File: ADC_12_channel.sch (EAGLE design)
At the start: 165 parts, among them K1 691131710003, K2 691101710002, K3 691101710002, K4 691101710002, K5 691101710002, K6 691101710002, K7 691101710002, K8 691101710002, K9 691101710002, U1 AD7864ASZ-1, U10 TL082D, U11 +12v, U12 V_REG_317SMD, U2 AD7864ASZ-1, U3 TL082D, U4 TL082D, U5 TL082D, U6 TL082D, U7 TL082D, U8 TL082D, U9 TL082D, X1 QTE-040

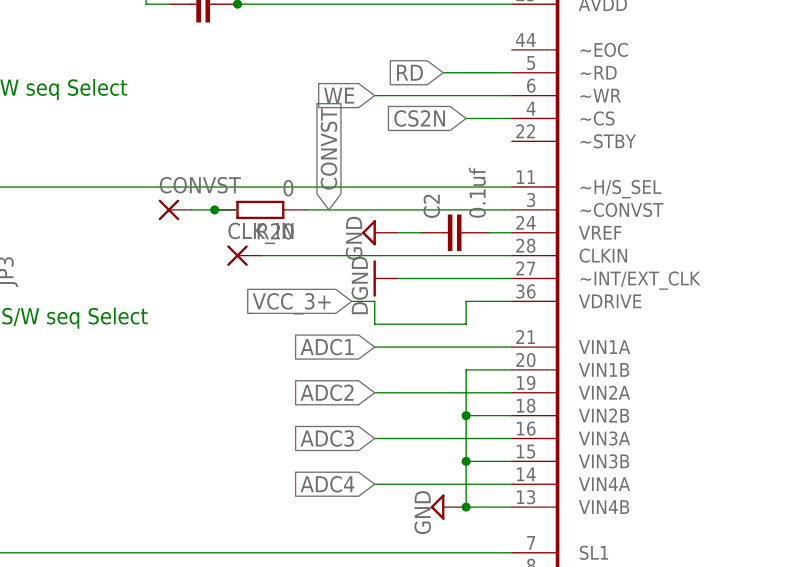
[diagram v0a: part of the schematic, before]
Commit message: Added CLK INT/EXT resistor & relocated inout Opamp
Reducing the size
created possibility to input external clock
relocated the Omapms to reduce the board size.
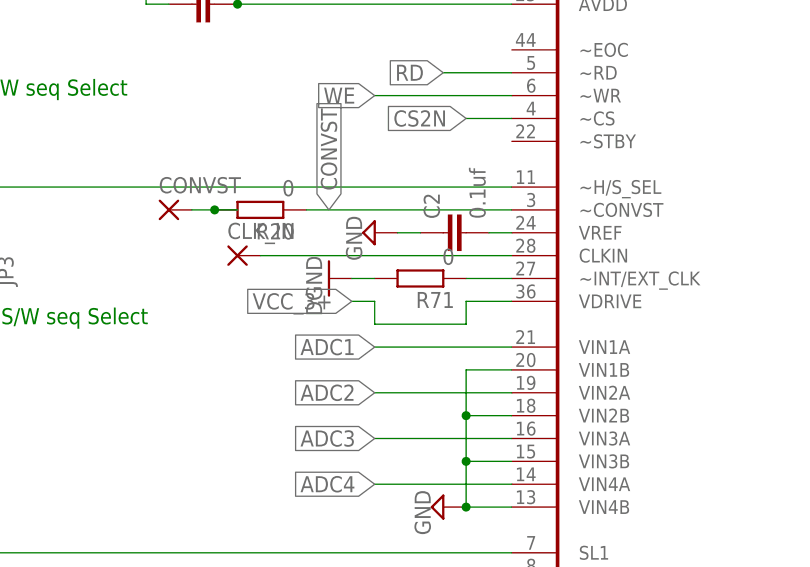
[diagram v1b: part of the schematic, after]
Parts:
- added R71: 0, resistor:R-EU_M1206
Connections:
- new net N$47: R71.1, U1.~INT/EXT_CLK
- net DGND: now also R71.2; no longer U1.~INT/EXT_CLK
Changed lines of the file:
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@@
 <part name="CONVST" library="wirepad" deviceset="3,17/1,3" device=""/>
 <part name="R20" library="resistor" deviceset="R-EU_" device="M1206" value="0"/>
+<part name="R71" library="resistor" deviceset="R-EU_" device="M1206" value="0"/>
 </parts>
 <sheets>
@@
 <instance part="AGND1" gate="GND" x="20.32" y="2.54" rot="R270"/>
 <instance part="AGND2" gate="GND" x="17.78" y="27.94" rot="R270"/>
-<instance part="GND6" gate="1" x="10.16" y="53.34" rot="R270"/>
+<instance part="GND6" gate="1" x="5.08" y="53.34" rot="R270"/>
 <instance part="SUPPLY3" gate="GND" x="10.16" y="58.42" rot="R270"/>
 <instance part="U$1" gate="G$1" x="617.22" y="274.32"/>
@@
 <instance part="CONVST" gate="1" x="-12.7" y="60.96"/>
 <instance part="R20" gate="G$1" x="-2.54" y="60.96" rot="R180"/>
+<instance part="R71" gate="G$1" x="15.24" y="53.34" rot="R180"/>
 </instances>
 <busses>
@@
 </segment>
 <segment>
-<pinref part="U1" gate="A" pin="~INT/EXT_CLK"/>
-<wire x1="25.4" y1="53.34" x2="12.7" y2="53.34" width="0.1524" layer="91"/>
-<pinref part="GND6" gate="1" pin="GND"/>
-</segment>
-<segment>
 <pinref part="C11" gate="G$1" pin="2"/>
 <pinref part="SUPPLY9" gate="GND" pin="GND"/>
@@
 <pinref part="SUPPLY18" gate="GND" pin="GND"/>
 <wire x1="-269.24" y1="-22.86" x2="-269.24" y2="-27.94" width="0.1524" layer="91"/>
+</segment>
+<segment>
+<pinref part="R71" gate="G$1" pin="2"/>
+<pinref part="GND6" gate="1" pin="GND"/>
+<wire x1="10.16" y1="53.34" x2="7.62" y2="53.34" width="0.1524" layer="91"/>
 </segment>
 </net>
@@
 </segment>
 </net>
+<net name="N$47" class="0">
+<segment>
+<pinref part="R71" gate="G$1" pin="1"/>
+<pinref part="U1" gate="A" pin="~INT/EXT_CLK"/>
+<wire x1="20.32" y1="53.34" x2="25.4" y2="53.34" width="0.1524" layer="91"/>
+</segment>
+</net>

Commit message: Removed unnecessary component Adjusted the location of ADC opamps Realigned Processors!! Very criticall
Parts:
- removed JP4: (no value), SparkFun-Retired:JUMPER-2PTH
- removed PAD2, PAD3: WIREPAD1,6/0,8, wirepad:WIREPAD1,6/0,8
- added R72: 0, resistor:R-EU_M1206
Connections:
- net DGND: now also R72.2; no longer JP4.1
- net N$25: now also R72.1; no longer JP4.2
- net VCC_12+: no longer PAD2.P
- net VCC_12-: no longer PAD3.P

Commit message: Removed Isolating 0 ohm resistors..
End of session commit
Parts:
- removed R71: 0, resistor:R-EU_M1206
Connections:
- removed net N$47: R71.1, U1.~INT/EXT_CLK
- net DGND: now also U1.~INT/EXT_CLK; no longer R71.2
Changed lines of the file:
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@@
 <part name="CONVST" library="wirepad" deviceset="3,17/1,3" device=""/>
 <part name="R20" library="resistor" deviceset="R-EU_" device="M1206" value="0"/>
-<part name="R71" library="resistor" deviceset="R-EU_" device="M1206" value="0"/>
 <part name="R72" library="resistor" deviceset="R-EU_" device="M1206" value="0"/>
 </parts>
@@
 <instance part="CONVST" gate="1" x="-12.7" y="60.96"/>
 <instance part="R20" gate="G$1" x="-2.54" y="60.96" rot="R180"/>
-<instance part="R71" gate="G$1" x="15.24" y="53.34" rot="R180"/>
 <instance part="R72" gate="G$1" x="-38.1" y="-111.76" rot="R180"/>
 </instances>
@@
 </segment>
 <segment>
-<pinref part="R71" gate="G$1" pin="2"/>
 <pinref part="GND6" gate="1" pin="GND"/>
-<wire x1="10.16" y1="53.34" x2="7.62" y2="53.34" width="0.1524" layer="91"/>
+<pinref part="U1" gate="A" pin="~INT/EXT_CLK"/>
+<wire x1="20.32" y1="53.34" x2="22.86" y2="53.34" width="0.1524" layer="91"/>
+<wire x1="22.86" y1="53.34" x2="25.4" y2="53.34" width="0.1524" layer="91"/>
+<wire x1="7.62" y1="53.34" x2="20.32" y2="53.34" width="0.1524" layer="91"/>
 </segment>
 </net>
@@
 </segment>
 </net>
-<net name="N$47" class="0">
-<segment>
-<pinref part="R71" gate="G$1" pin="1"/>
-<pinref part="U1" gate="A" pin="~INT/EXT_CLK"/>
-<wire x1="20.32" y1="53.34" x2="25.4" y2="53.34" width="0.1524" layer="91"/>
-</segment>
-</net>

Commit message: Restore pint - 2 Moved ADC chip connected the two resistors
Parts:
- added R71: 0, resistor:R-EU_M1206
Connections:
- new net N$47: C20.+, C59.1, R17.1, U$1.OUT
- net VCC_12+: no longer C20.+, C59.1, R17.1, U$1.OUT
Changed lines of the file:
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@@
 <part name="R20" library="resistor" deviceset="R-EU_" device="M1206" value="0"/>
 <part name="R72" library="resistor" deviceset="R-EU_" device="M1206" value="0"/>
+<part name="R71" library="resistor" deviceset="R-EU_" device="M1206" value="0"/>
 </parts>
 <sheets>
@@
 <instance part="R20" gate="G$1" x="-2.54" y="60.96" rot="R180"/>
 <instance part="R72" gate="G$1" x="-38.1" y="-111.76" rot="R180"/>
+<instance part="R71" gate="G$1" x="640.08" y="284.48" rot="R270"/>
 </instances>
 <busses>
@@
 <net name="VCC_12+" class="0">
 <segment>
-<pinref part="C20" gate="G$1" pin="+"/>
-<wire x1="629.92" y1="274.32" x2="635" y2="274.32" width="0.1524" layer="91"/>
-<wire x1="635" y1="274.32" x2="635" y2="269.24" width="0.1524" layer="91"/>
-<pinref part="R17" gate="G$1" pin="1"/>
-<wire x1="635" y1="274.32" x2="642.62" y2="274.32" width="0.1524" layer="91"/>
-<junction x="635" y="274.32"/>
-<wire x1="642.62" y1="274.32" x2="645.16" y2="274.32" width="0.1524" layer="91"/>
-<wire x1="645.16" y1="274.32" x2="655.32" y2="274.32" width="0.1524" layer="91"/>
-<wire x1="642.62" y1="269.24" x2="642.62" y2="274.32" width="0.1524" layer="91"/>
-<junction x="642.62" y="274.32"/>
 <label x="645.16" y="279.4" size="1.778" layer="95" rot="R90" xref="yes"/>
-<wire x1="645.16" y1="274.32" x2="645.16" y2="281.94" width="0.1524" layer="91"/>
-<junction x="645.16" y="274.32"/>
 <wire x1="645.16" y1="281.94" x2="678.18" y2="281.94" width="0.1524" layer="91"/>
 <pinref part="C28" gate="G$1" pin="+"/>
@@
 <wire x1="678.18" y1="276.86" x2="678.18" y2="281.94" width="0.1524" layer="91"/>
 <junction x="678.18" y="281.94"/>
-<pinref part="U$1" gate="G$1" pin="OUT"/>
-<pinref part="C59" gate="G$1" pin="1"/>
 <pinref part="U12" gate="G$1" pin="IN"/>
 </segment>
@@
 </segment>
 </net>
+<net name="N$47" class="0">
+<segment>
+<pinref part="R17" gate="G$1" pin="1"/>
+<wire x1="642.62" y1="274.32" x2="655.32" y2="274.32" width="0.1524" layer="91"/>
+<pinref part="C59" gate="G$1" pin="1"/>
+<wire x1="642.62" y1="269.24" x2="642.62" y2="274.32" width="0.1524" layer="91"/>
+<junction x="642.62" y="274.32"/>
+<pinref part="C20" gate="G$1" pin="+"/>
+<wire x1="635" y1="274.32" x2="635" y2="269.24" width="0.1524" layer="91"/>
+<wire x1="635" y1="274.32" x2="642.62" y2="274.32" width="0.1524" layer="91"/>
+<junction x="635" y="274.32"/>
+<wire x1="629.92" y1="274.32" x2="635" y2="274.32" width="0.1524" layer="91"/>
+<pinref part="U$1" gate="G$1" pin="OUT"/>
+</segment>
+</net>

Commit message: Added a voltage divider for 3V supply corrected the VDD and AVDD mess-up
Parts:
- added R73: 0, resistor:R-EU_M1206
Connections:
- removed net N$47: C20.+, C59.1, R17.1, U$1.OUT
- new net 5V: C28.+, R71.1, R73.2, U12.IN
- net GND2: now also R73.1
- net VCC_12+: now also C20.+, C59.1, R17.1, R71.2, U$1.OUT; no longer C28.+, U12.IN
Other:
- moved on the sheet: R71
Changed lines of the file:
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@@
 <part name="R72" library="resistor" deviceset="R-EU_" device="M1206" value="0"/>
 <part name="R71" library="resistor" deviceset="R-EU_" device="M1206" value="0"/>
+<part name="R73" library="resistor" deviceset="R-EU_" device="M1206" value="0"/>
 </parts>
 <sheets>
@@
 <instance part="R20" gate="G$1" x="-2.54" y="60.96" rot="R180"/>
 <instance part="R72" gate="G$1" x="-38.1" y="-111.76" rot="R180"/>
-<instance part="R71" gate="G$1" x="640.08" y="284.48" rot="R270"/>
+<instance part="R71" gate="G$1" x="645.16" y="279.4" rot="R270"/>
+<instance part="R73" gate="G$1" x="650.24" y="261.62" rot="R90"/>
 </instances>
 <busses>
@@
 <net name="VCC_12+" class="0">
 <segment>
-<label x="645.16" y="279.4" size="1.778" layer="95" rot="R90" xref="yes"/>
-<wire x1="645.16" y1="281.94" x2="678.18" y2="281.94" width="0.1524" layer="91"/>
-<pinref part="C28" gate="G$1" pin="+"/>
-<wire x1="678.18" y1="281.94" x2="680.72" y2="281.94" width="0.1524" layer="91"/>
-<wire x1="678.18" y1="276.86" x2="678.18" y2="281.94" width="0.1524" layer="91"/>
-<junction x="678.18" y="281.94"/>
-<pinref part="U12" gate="G$1" pin="IN"/>
-</segment>
-<segment>
 <pinref part="U3" gate="P" pin="V+"/>
 <wire x1="-274.32" y1="127" x2="-274.32" y2="129.54" width="0.1524" layer="91"/>
@@
 <wire x1="-287.02" y1="-411.48" x2="-287.02" y2="-408.94" width="0.1524" layer="91"/>
 <junction x="-287.02" y="-411.48"/>
+</segment>
+<segment>
+<pinref part="R17" gate="G$1" pin="1"/>
+<wire x1="642.62" y1="274.32" x2="645.16" y2="274.32" width="0.1524" layer="91"/>
+<pinref part="C59" gate="G$1" pin="1"/>
+<wire x1="645.16" y1="274.32" x2="655.32" y2="274.32" width="0.1524" layer="91"/>
+<wire x1="642.62" y1="269.24" x2="642.62" y2="274.32" width="0.1524" layer="91"/>
+<junction x="642.62" y="274.32"/>
+<pinref part="C20" gate="G$1" pin="+"/>
+<wire x1="635" y1="274.32" x2="635" y2="269.24" width="0.1524" layer="91"/>
+<wire x1="635" y1="274.32" x2="642.62" y2="274.32" width="0.1524" layer="91"/>
+<junction x="635" y="274.32"/>
+<wire x1="629.92" y1="274.32" x2="635" y2="274.32" width="0.1524" layer="91"/>
+<pinref part="U$1" gate="G$1" pin="OUT"/>
+<pinref part="R71" gate="G$1" pin="2"/>
+<junction x="645.16" y="274.32"/>
+<label x="640.08" y="279.4" size="1.778" layer="95" rot="R90" xref="yes"/>
 </segment>
 </net>
@@
 <junction x="642.62" y="256.54"/>
 <pinref part="LED5" gate="G$1" pin="C"/>
-<wire x1="642.62" y1="256.54" x2="673.1" y2="256.54" width="0.1524" layer="91"/>
+<wire x1="642.62" y1="256.54" x2="650.24" y2="256.54" width="0.1524" layer="91"/>
+<wire x1="650.24" y1="256.54" x2="673.1" y2="256.54" width="0.1524" layer="91"/>
 <wire x1="673.1" y1="256.54" x2="673.1" y2="261.62" width="0.1524" layer="91"/>
 <pinref part="LED6" gate="G$1" pin="C"/>
@@
 <pinref part="C22" gate="G$1" pin="1"/>
 <pinref part="U12" gate="G$1" pin="ADJ"/>
+<pinref part="R73" gate="G$1" pin="1"/>
+<junction x="650.24" y="256.54"/>
 </segment>
 </net>
@@
 </segment>
 </net>
-<net name="N$47" class="0">
-<segment>
-<pinref part="R17" gate="G$1" pin="1"/>
-<wire x1="642.62" y1="274.32" x2="655.32" y2="274.32" width="0.1524" layer="91"/>
-<pinref part="C59" gate="G$1" pin="1"/>
-<wire x1="642.62" y1="269.24" x2="642.62" y2="274.32" width="0.1524" layer="91"/>
-<junction x="642.62" y="274.32"/>
-<pinref part="C20" gate="G$1" pin="+"/>
-<wire x1="635" y1="274.32" x2="635" y2="269.24" width="0.1524" layer="91"/>
-<wire x1="635" y1="274.32" x2="642.62" y2="274.32" width="0.1524" layer="91"/>
-<junction x="635" y="274.32"/>
-<wire x1="629.92" y1="274.32" x2="635" y2="274.32" width="0.1524" layer="91"/>
-<pinref part="U$1" gate="G$1" pin="OUT"/>
-</segment>
-</net>
+<net name="5V" class="0">
+<segment>
+<pinref part="C28" gate="G$1" pin="+"/>
+<wire x1="678.18" y1="281.94" x2="680.72" y2="281.94" width="0.1524" layer="91"/>
+<wire x1="678.18" y1="276.86" x2="678.18" y2="281.94" width="0.1524" layer="91"/>
+<pinref part="U12" gate="G$1" pin="IN"/>
+<pinref part="R71" gate="G$1" pin="1"/>
+<pinref part="R73" gate="G$1" pin="2"/>
+<wire x1="645.16" y1="284.48" x2="650.24" y2="284.48" width="0.1524" layer="91"/>
+<wire x1="650.24" y1="284.48" x2="650.24" y2="281.94" width="0.1524" layer="91"/>
+<wire x1="650.24" y1="281.94" x2="650.24" y2="266.7" width="0.1524" layer="91"/>
+<wire x1="678.18" y1="281.94" x2="650.24" y2="281.94" width="0.1524" layer="91"/>
+<junction x="678.18" y="281.94"/>
+<junction x="650.24" y="281.94"/>
+</segment>
+</net>

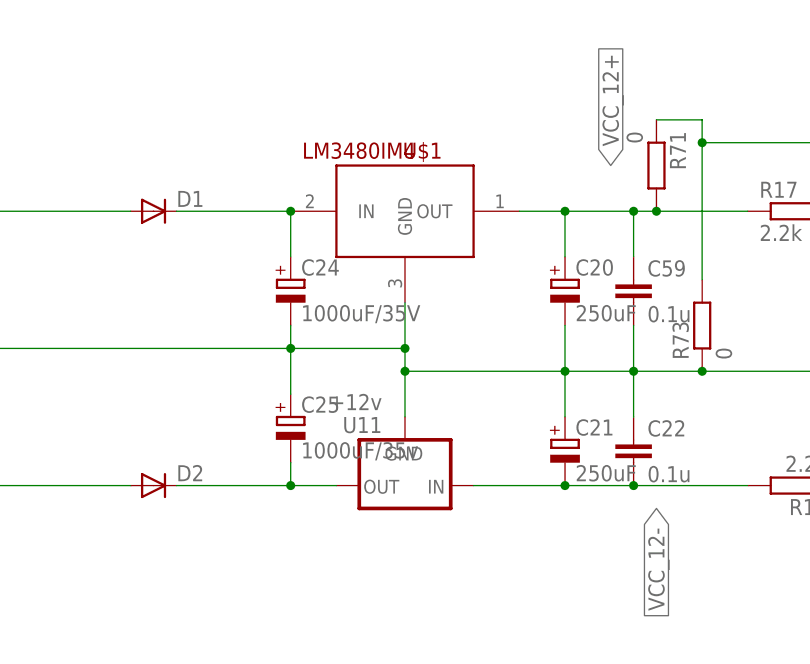
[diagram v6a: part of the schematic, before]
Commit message: Supply sorting commit
Sorted I/p +- 12V supply, 5V pending
changed Resistor package from 0805 to 1206 because its cheap, easy to handle, and easyly available

Update of R package done for 1st two input channels
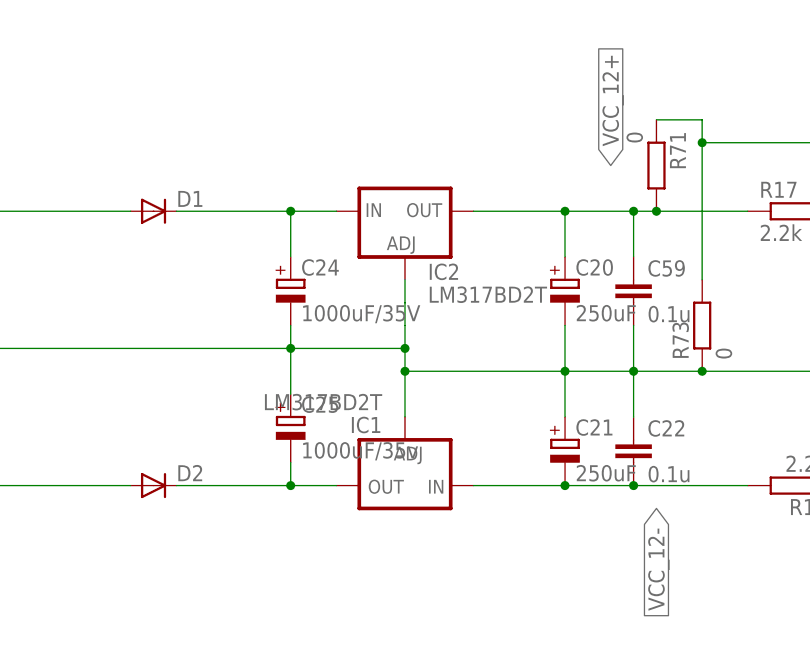
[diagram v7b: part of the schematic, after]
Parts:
- removed U$1: LM3480IM4, SparkFun-PowerIC:LM3480IM4
- removed U11: +12v, rathin_lib:V_REG_78XX7912
- added IC1: LM317BD2T, rathin_Vreg_D2pack:LM317BD2T
- added IC2: LM317BD2T, v-reg:LM317BD2T
- R11, R12, R13, R14, R15, R16, R24, R25, R26, R31, R36, R37: device resistor:R-EU_M0805 -> resistor:R-EU_M1206
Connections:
- net GND2: now also IC1.ADJ, IC2.ADJ; no longer U$1.GND, U11.GND
- net N$35: now also IC1.OUT; no longer U11.OUT
- net N$36: now also IC2.IN; no longer U$1.IN
- net VCC_12+: now also IC2.OUT; no longer U$1.OUT
- net VCC_12-: now also IC1.IN; no longer U11.IN

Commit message: R & C package update
Updated all R to 1206
Updated all input stage C of 0.1u to 0603 package
All 47uF to 1206 package
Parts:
- removed JP2, JP3, JP5: (no value), SparkFun-Retired:JUMPER-2PTH
- added R74: 0, resistor:R-EU_M1206
- C1, C10, C11, C12, C13, C14, C15, C16, C17, C18, C19, C2, C22, C30, C31, C32, C33, C34, C35, C36, C37, C38, C39, C40, C41, C42, C43, C44, C45, C46, C47, C48, C49, C5, C50, C51, C52, C53, C54, C55, C56, C57, C58, C59, C6, C9: device rcl:C-EUC0805 -> rcl:C-EUC0603K
- C4, C8: device rcl:C-EUC0603K -> rcl:C-EUC1206K
- R10, R27, R28, R29, R30, R32, R33, R34, R35, R38, R39, R40, R41, R42, R43, R44, R45, R47, R48, R49, R50, R51, R53, R54, R55, R56, R57, R59, R60, R61, R62, R63, R64, R65: device resistor:R-EU_M0805 -> resistor:R-EU_M1206
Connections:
- removed net N$18: JP2.2, JP3.1, U1.~H/S_SEL
- removed net N$25: JP5.1, R72.1, U2.~H/S_SEL
- net DGND: now also R74.2; no longer JP2.1
- net N$19: now also R74.1, U1.~H/S_SEL; no longer JP3.2
- net N$26: now also R72.1, U2.~H/S_SEL; no longer JP5.2
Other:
- note added: "DO NOT connect!"
- note removed: "For S/W seq Select"
